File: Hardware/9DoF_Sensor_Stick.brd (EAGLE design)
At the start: 22.9 x 10.2 mm, 19 parts, among them U1 LSM9DS1

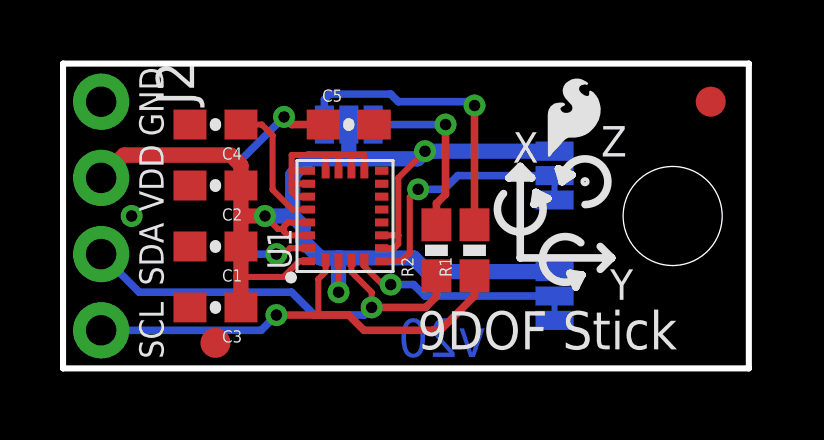
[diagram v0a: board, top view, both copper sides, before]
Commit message: v20 Changes
- Switch to micro fiducials for better clearances.
- Changed default I2C addresses to ox1E and 0x6B to match example code
for LSM9DS1 Breakout.
- Moved "v20" bottom copper text to clear bottom silk
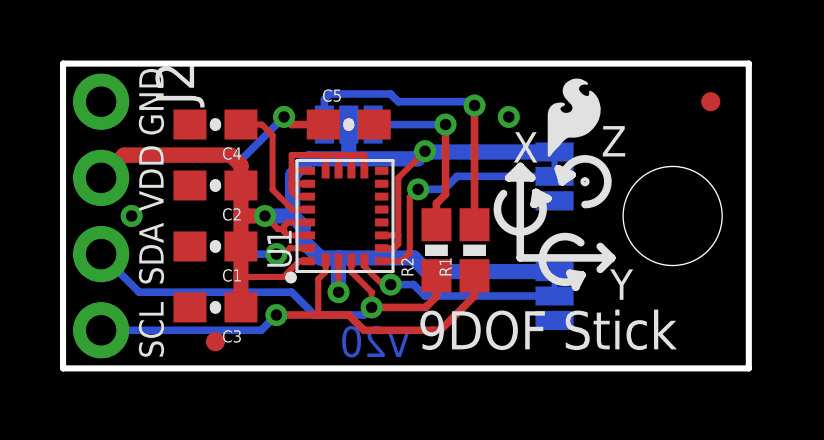
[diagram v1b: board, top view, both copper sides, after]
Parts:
- removed FD1, FD2: FIDUCIAL1X2, SparkFun-Aesthetics:FIDUCIAL-1X2
- removed U$1: REVISION, SparkFun-Aesthetics:REVISION
- added FD3, FD4: FIDUCIALUFIDUCIAL, SparkFun-Aesthetics:MICRO-FIDUCIAL
- turned JP3 to 90 degrees
- turned JP2 to 90 degrees
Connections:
- net GND: now also JP2.1, JP3.1; no longer JP2.3, JP3.3
- net VDD: now also JP2.3, JP3.3; no longer JP2.1, JP3.1
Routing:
- net GND: vias 1 -> 2
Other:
- board text removed: "C. Taylor and N. Seidle"
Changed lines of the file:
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@@
 <grid distance="0.05" unitdist="inch" unit="inch" style="lines" multiple="1" display="yes" altdistance="0.005" altunitdist="inch" altunit="inch"/>
 <layers>
-<layer number="1" name="Top" color="4" fill="1" visible="yes" active="yes"/>
+<layer number="1" name="Top" color="4" fill="1" visible="no" active="yes"/>
 <layer number="2" name="Route2" color="1" fill="3" visible="no" active="no"/>
 <layer number="3" name="Route3" color="4" fill="3" visible="no" active="no"/>
@@
 <layer number="19" name="Unrouted" color="6" fill="1" visible="yes" active="yes"/>
 <layer number="20" name="Dimension" color="15" fill="1" visible="yes" active="yes"/>
-<layer number="21" name="tPlace" color="16" fill="1" visible="yes" active="yes"/>
+<layer number="21" name="tPlace" color="16" fill="1" visible="no" active="yes"/>
 <layer number="22" name="bPlace" color="14" fill="1" visible="yes" active="yes"/>
 <layer number="23" name="tOrigins" color="15" fill="1" visible="yes" active="yes"/>
@@
 <text x="2.54" y="6.985" size="1.016" layer="22" font="vector" ratio="15" rot="MR180" align="center-left">1.9-</text>
 <text x="2.54" y="5.715" size="1.016" layer="22" font="vector" ratio="15" rot="MR180" align="center-left">3.6V</text>
-<text x="21.717" y="-17.907" size="1.778" layer="51" font="vector" ratio="15">C. Taylor and N. Seidle</text>
-<text x="21.59" y="-21.59" size="1.778" layer="51" font="vector" ratio="15">Alex Wende</text>
-<text x="14.097" y="0.381" size="1.27" layer="16" font="vector" ratio="15" rot="MR0">v20</text>
+<text x="21.59" y="-17.78" size="1.778" layer="51" font="vector" ratio="15">Alex Wende</text>
+<text x="11.557" y="0.381" size="1.016" layer="16" font="vector" ratio="15" rot="MR0">v20</text>
 <dimension x1="0" y1="10.16" x2="22.86" y2="10.16" x3="11.43" y3="15.239996875" textsize="1.27" textratio="15" layer="47" unit="inch"/>
 <dimension x1="22.86" y1="0" x2="22.86" y2="5.08" x3="27.94" y3="2.54" textsize="1.27" textratio="15" layer="47" unit="inch"/>
@@
 <dimension x1="0" y1="0" x2="0" y2="10.16" x3="-5.08" y3="5.08" textsize="1.27" textratio="15" layer="47" unit="inch" precision="3"/>
 <text x="2.54" y="20.32" size="1.27" layer="47" font="vector" ratio="15">Units are in Inches</text>
-<text x="33.02" y="7.62" size="1.27" layer="51" font="vector" ratio="15">PCB thickness = 0.032"</text>
+<text x="30.48" y="3.81" size="1.27" layer="51" font="vector" ratio="15">PCB thickness = 0.032"</text>
 </plain>
 <attributes>
@@
 <attribute name="PROD_ID" value="CAP-00810" x="9.525" y="8.128" size="1.778" layer="27" display="off"/>
 </element>
-<element name="FD1" library="SparkFun-Aesthetics" package="FIDUCIAL-1X2" value="FIDUCIAL1X2" x="21.59" y="8.89"/>
-<element name="FD2" library="SparkFun-Aesthetics" package="FIDUCIAL-1X2" value="FIDUCIAL1X2" x="5.08" y="0.8509"/>
 <element name="FRAME1" library="SparkFun-Aesthetics" package="CREATIVE_COMMONS" value="FRAME-LETTER" x="-10.16" y="-17.78"/>
 <element name="H1" library="SparkFun-Electromechanical" package="STAND-OFF" value="STAND-OFF" x="20.32" y="5.08"/>
@@
 <attribute name="PROD_ID" value="RES-07857" x="12.446" y="3.937" size="1.778" layer="27" rot="R90" display="off"/>
 </element>
-<element name="U$1" library="SparkFun-Aesthetics" package="REVISION" value="REVISION" x="1.27" y="-21.59"/>
 <element name="U1" library="SparkFun-Sensors" package="LGA24-8X4" value="LSM9DS1" x="9.398" y="5.08" rot="R90">
 <attribute name="PROD_ID" value="IC-12536" x="9.398" y="5.08" size="1.778" layer="27" rot="R90" display="off"/>
 </element>
-<element name="JP2" library="SparkFun-Passives" package="PAD-JUMPER-3-2OF3_NC_BY_TRACE_YES_SILK_FULL_BOX" value="" x="16.383" y="2.413" rot="MR270"/>
-<element name="JP3" library="SparkFun-Passives" package="PAD-JUMPER-3-2OF3_NC_BY_TRACE_YES_SILK_FULL_BOX" value="" x="16.383" y="6.4262" rot="MR270"/>
+<element name="JP2" library="SparkFun-Passives" package="PAD-JUMPER-3-2OF3_NC_BY_TRACE_YES_SILK_FULL_BOX" value="" x="16.383" y="2.413" rot="MR90"/>
+<element name="JP3" library="SparkFun-Passives" package="PAD-JUMPER-3-2OF3_NC_BY_TRACE_YES_SILK_FULL_BOX" value="" x="16.383" y="6.4008" rot="MR90"/>
+<element name="FD3" library="SparkFun-Aesthetics" package="MICRO-FIDUCIAL" value="FIDUCIALUFIDUCIAL" x="5.08" y="0.889"/>
+<element name="FD4" library="SparkFun-Aesthetics" package="MICRO-FIDUCIAL" value="FIDUCIALUFIDUCIAL" x="21.59" y="8.89"/>
 </elements>
 <signals>
@@
 <contactref element="R2" pad="2"/>
 <via x="12.7508" y="8.128" extent="1-16" drill="0.381"/>
-<wire x1="10.3378" y1="8.128" x2="12.7508" y2="8.128" width="0.254" layer="16"/>
 <wire x1="12.7508" y1="8.128" x2="12.7508" y2="5.802859375" width="0.254" layer="1"/>
 <wire x1="12.446" y1="5.498059375" x2="12.446" y2="4.787" width="0.254" layer="1"/>
 <wire x1="12.446" y1="5.498059375" x2="12.7508" y2="5.802859375" width="0.254" layer="1"/>
+<wire x1="10.3378" y1="8.128" x2="12.7508" y2="8.128" width="0.254" layer="16"/>
 </signal>
 <signal name="N$2">
@@
 <wire x1="8.7122" y1="8.128" x2="8.7122" y2="8.9662" width="0.254" layer="16"/>
 <wire x1="8.7122" y1="8.9662" x2="8.89" y2="9.144" width="0.254" layer="16"/>
-<wire x1="13.716" y1="8.763" x2="13.716" y2="8.89" width="0.254" layer="16"/>
 <wire x1="13.716" y1="8.89" x2="11.176" y2="8.89" width="0.254" layer="16"/>
 <wire x1="11.176" y1="8.89" x2="10.922" y2="9.144" width="0.254" layer="16"/>
 <wire x1="10.922" y1="9.144" x2="8.89" y2="9.144" width="0.254" layer="16"/>
 <wire x1="13.716" y1="8.763" x2="13.716" y2="4.787" width="0.254" layer="1"/>
+<wire x1="13.716" y1="8.763" x2="13.716" y2="8.89" width="0.254" layer="16"/>
 </signal>
 <signal name="SCL">
@@
 <contactref element="U1" pad="8"/>
 <contactref element="U1" pad="7"/>
-<contactref element="JP2" pad="1"/>
-<contactref element="JP3" pad="1"/>
 <wire x1="9.525" y1="8.128" x2="9.525" y2="6.985" width="0.508" layer="16"/>
 <wire x1="9.525" y1="6.985" x2="8.19195" y2="6.985" width="0.508" layer="16"/>
@@
 <wire x1="11.176" y1="4.435" x2="10.623" y2="4.435" width="0.2032" layer="1"/>
 <wire x1="7.161" y1="4.65" x2="6.731" y2="5.08" width="0.2032" layer="1"/>
-<wire x1="12.065" y1="7.239" x2="11.811" y2="6.985" width="0.508" layer="16"/>
 <wire x1="11.811" y1="6.985" x2="9.525" y2="6.985" width="0.508" layer="16"/>
-<wire x1="16.383" y1="3.2258" x2="12.1412" y2="3.2258" width="0.508" layer="16"/>
 <wire x1="12.1412" y1="3.2258" x2="11.684" y2="3.683" width="0.508" layer="16"/>
 <wire x1="11.684" y1="3.683" x2="9.183" y2="3.683" width="0.508" layer="16"/>
 <wire x1="9.183" y1="2.54" x2="9.183" y2="3.683" width="0.508" layer="16"/>
 <wire x1="9.183" y1="3.605" x2="9.183" y2="2.54" width="0.2032" layer="1"/>
-<wire x1="16.383" y1="7.239" x2="12.065" y2="7.239" width="0.508" layer="16"/>
+<contactref element="JP2" pad="3"/>
+<contactref element="JP3" pad="3"/>
+<wire x1="16.383" y1="7.2136" x2="12.0904" y2="7.2136" width="0.508" layer="16"/>
+<wire x1="12.0904" y1="7.2136" x2="12.065" y2="7.239" width="0.508" layer="16"/>
+<wire x1="16.383" y1="3.2258" x2="12.1412" y2="3.2258" width="0.508" layer="16"/>
+<wire x1="12.065" y1="7.239" x2="11.811" y2="6.985" width="0.508" layer="16"/>
 </signal>
 <signal name="N$5">
@@
 </polygon>
 <via x="2.286" y="5.08" extent="1-16" drill="0.381"/>
-<contactref element="JP2" pad="3"/>
 <wire x1="8.753" y1="7.112" x2="9.183" y2="7.112" width="0.2032" layer="1"/>
-<contactref element="JP3" pad="3"/>
+<contactref element="JP2" pad="1"/>
+<contactref element="JP3" pad="1"/>
+<via x="14.859" y="8.382" extent="1-16" drill="0.381"/>
 </signal>
 <signal name="SDO_A/G">
@@
 <wire x1="11.557" y1="5.715" x2="11.8364" y2="5.9944" width="0.2032" layer="1"/>
 <wire x1="11.8364" y1="5.9944" x2="11.8364" y2="5.969" width="0.2032" layer="1"/>
-<wire x1="16.383" y1="6.4262" x2="13.1572" y2="6.4262" width="0.254" layer="16"/>
-<wire x1="13.1572" y1="6.4262" x2="12.7" y2="5.969" width="0.254" layer="16"/>
 <wire x1="12.7" y1="5.969" x2="11.8364" y2="5.969" width="0.254" layer="16"/>
+<wire x1="16.383" y1="6.4008" x2="13.1318" y2="6.4008" width="0.254" layer="16"/>
+<wire x1="13.1318" y1="6.4008" x2="12.7" y2="5.969" width="0.254" layer="16"/>
 </signal>
 </signals>
